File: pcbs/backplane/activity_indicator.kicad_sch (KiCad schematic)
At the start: 7 parts, among them U30 LTC6993xS6-2

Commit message: Backplane comms updates, manufacturing renaming
Removed misspelled "maunfacturing" folder, fixed gitignore rule to remove manufacturing folders within individual PCB folders too
Changed SCKI/SCKO terminology to SCK, SCK_LB (loopback) for clarity
Added ADC_CS loopback signal between amp ctrl board & backplane for better fast-clock timing (#38)
Backplane: changed LVDS FPGA outputs to single-ended FPGA outputs to gain more I/O pins, added external LVDS transceivers (#38)
Backplane: replaced global clock & ~LDAC buffers with a separate FPGA pin for each amp ctrl board (#38)
Backplane: removed +2.5V power supply and level translations, no longer needed without FPGA I/O pins using LVDS_25 I/O configuration
Backplane: replaced +VDC-input resistor with solder jumper (on by default)
Backplane: changed field names (Part Number to MPN) to match Aisler's naming convention for automatic recognition
Amp ctrl: fixed optional level-shifter circuit on each channel for voltage inputs (#9) schematic & channel-1 layout
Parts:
- C63: MPN (none) -> C0603C104K5RACTU; Part Number C0603C104K5RACTU -> (none)
- D13: MPN (none) -> LTST-C170KSKT; Part Number LTST-C170KSKT -> (none)
- R47: MPN (none) -> RK73H2ATTD1002F; Part Number RK73H2ATTD1002F -> (none)
- R48: MPN (none) -> RK73H2ATTD6811F; Part Number RK73H2ATTD6811F -> (none)
- R49: MPN (none) -> RK73H2ATTD1802F; Part Number RK73H2ATTD1802F -> (none)
- R50: MPN (none) -> RK73H2ATTD1001F; Part Number RK73H2ATTD1001F -> (none)
- U30: MPN (none) -> LTC6993CS6-2#TRMPBF; MPN Alt. (none) -> LTC6993IS6-2#TRMPBF; Part Number LTC6993CS6-2#TRMPBF -> (none); Part Number Alt. LTC6993IS6-2#TRMPBF -> (none)

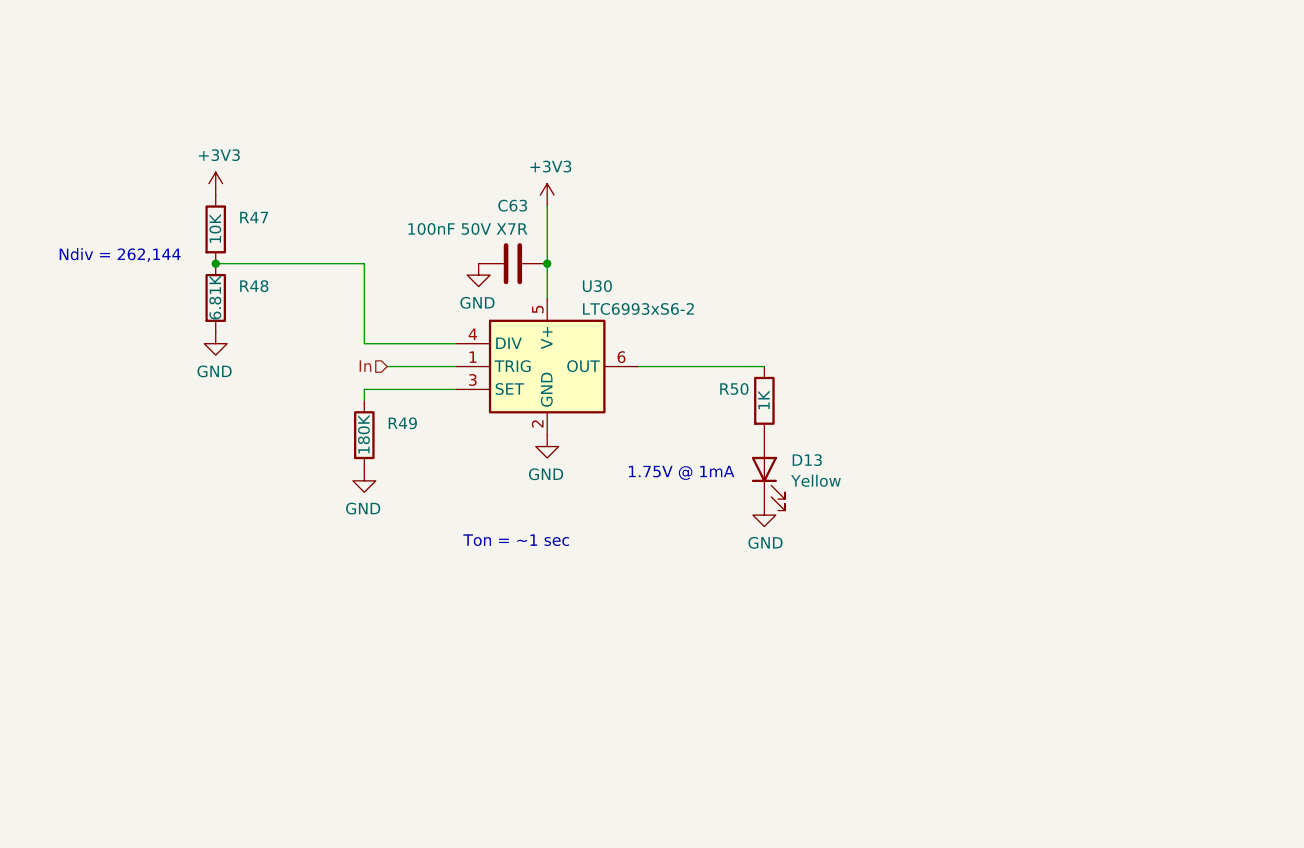
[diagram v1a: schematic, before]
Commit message: Backplane: changed timer ICs to TLC556 (fixes #45)
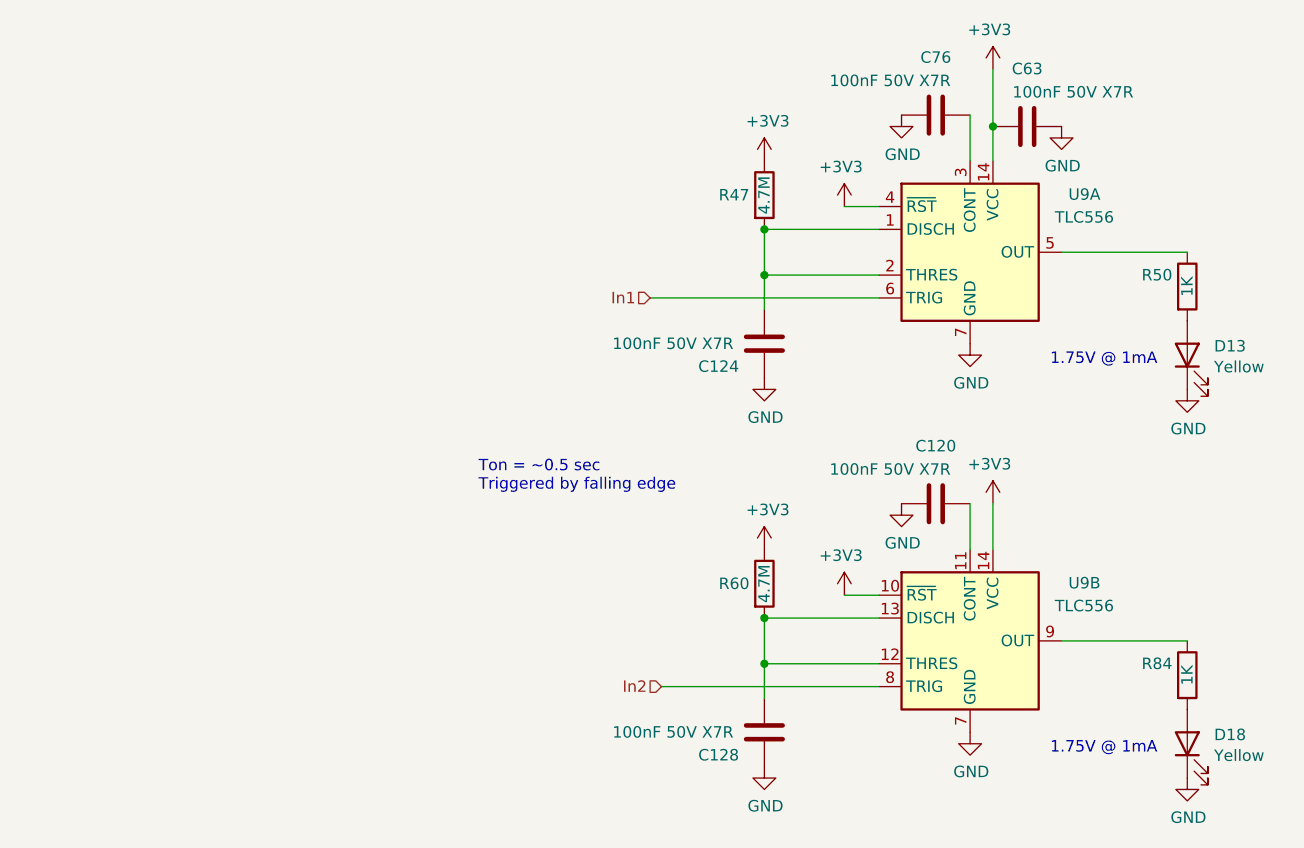
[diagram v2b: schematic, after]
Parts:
- removed R48: 6.81K, Resistor_SMD:R_0805_2012Metric, symbol Device:R
- removed R49: 180K, Resistor_SMD:R_0805_2012Metric, symbol Device:R
- removed U30: LTC6993xS6-2, Package_TO_SOT_SMD:TSOT-23-6, symbol Timer:LTC6993xS6-1
- added C120, C124, C128, C76: 100nF 50V X7R, Capacitor_SMD:C_0603_1608Metric, symbol Device:C
- added D18: Yellow, LED_SMD:LED_0805_2012Metric, symbol Device:LED
- added R60: 4.7M, Resistor_SMD:R_0805_2012Metric, symbol Device:R
- added R84: 1K, Resistor_SMD:R_0805_2012Metric, symbol Device:R
- added U9: TLC556, Package_SO:SOIC-14_3.9x8.7mm_P1.27mm, symbol Timer:LM556
- R47: value 10K -> 4.7M; MPN RK73H2ATTD1002F -> RK73H2ATTD4704F
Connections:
- net +3V3: now also R60.1, U9.10 (~{RST}), U9.14 (VCC), U9.14 (VCC), U9.4 (~{RST})
- net GND: now also C120.1, C124.2, C128.2, C76.1, D18.1 (K), U9.7 (GND), U9.7 (GND)
- net at R47.2: now also C124.1, U9.1 (DISCH), U9.2 (THRES)
- net at R50.1: now also U9.5 (OUT)
- new net: D18.2 (A), R84.2
- new net: C76.2, U9.3 (CONT)
- new net: C128.1, R60.2, U9.12 (THRES), U9.13 (DISCH)
- new net: C120.2, U9.11 (CONT)
- new net: R84.1, U9.9 (OUT)
- new net In1: U9.6 (TRIG)
- new net In2: U9.8 (TRIG)
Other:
- note added: "Ton = ~0.5 sec Triggered by falling edge"
- note removed: "Ndiv = 262,144"
- note removed: "Ton = ~1 sec"
- moved on the sheet: C63, D13, R47, R50
